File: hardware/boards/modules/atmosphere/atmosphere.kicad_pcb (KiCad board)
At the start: 2 copper layers, 95 x 75 mm, 18 parts, among them U7 ATtiny1614, U8 buffer

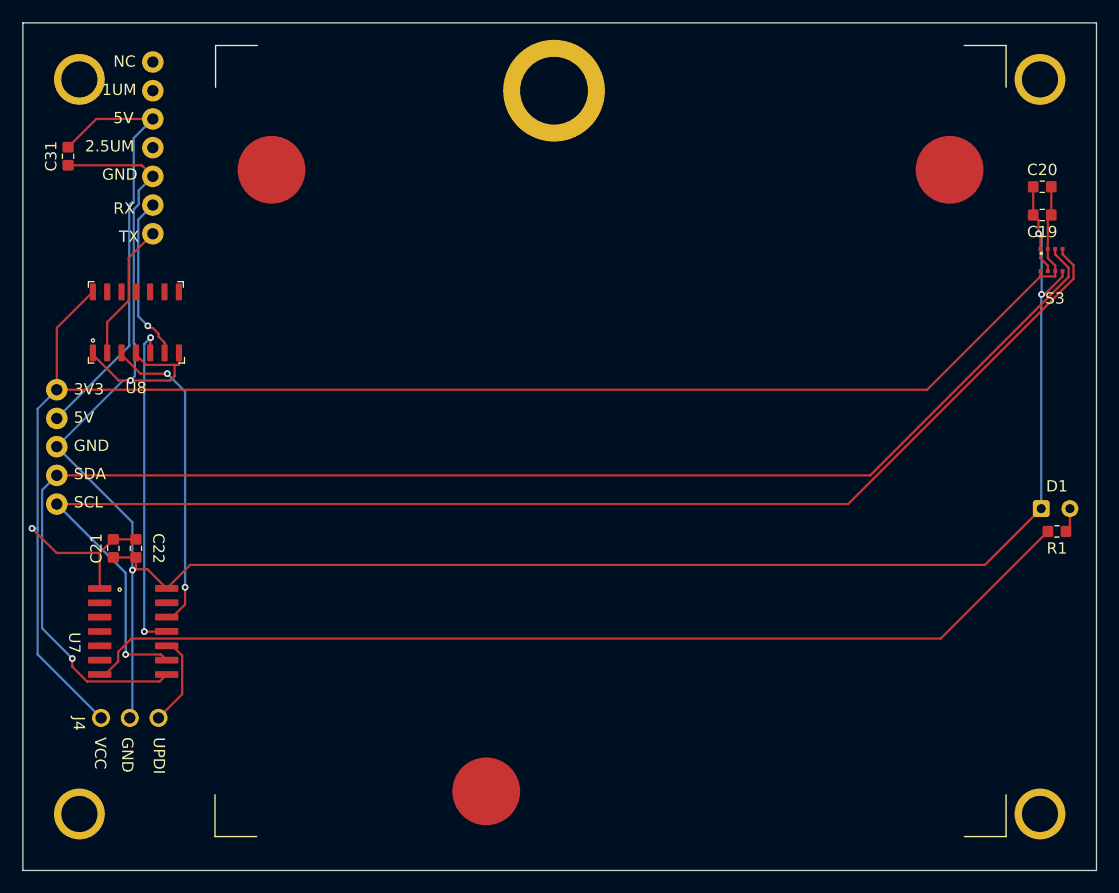
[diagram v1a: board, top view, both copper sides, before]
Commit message: updated sensor module schematics
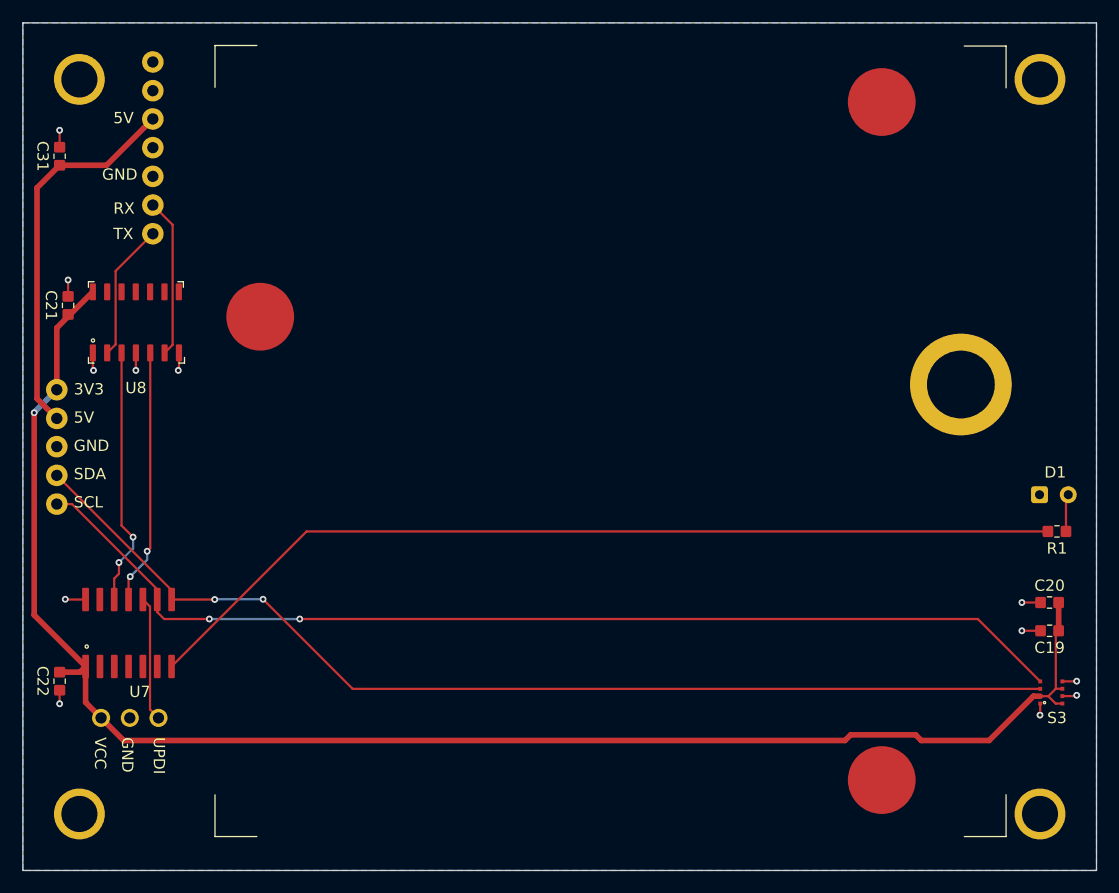
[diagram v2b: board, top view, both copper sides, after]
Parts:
- moved S3 38.3 mm to (203.0, 125.2), turned to 90 degrees
- moved C19 36.8 mm to (202.8, 119.8)
- moved C20 36.8 mm to (202.8, 117.3)
- moved C21 21.9 mm to (116.0, 91.0), turned to -90 degrees
- moved C22 13.6 mm to (115.2, 124.2)
- moved U7 7.93 mm to (122.3, 125.7), turned to 0 degrees
- moved D1 1.24 mm to (203.3, 110.8)
- moved C31 0.75 mm to (115.2, 77.8), turned to -90 degrees
- turned REF** to -90 degrees
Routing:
- net GND: track 200.1 -> 17.6 mm, vias 4 -> 12
- net SDA: track 127.5 -> 95.3 mm, vias 1 -> 2
- net SCL: track 120.9 -> 94.7 mm, vias 1 -> 2
- net 3V3: track 157.6 -> 142.7 mm
- net STATUS_LED: track 89.6 -> 82.5 mm
- net AT_CLIM_TX: track 29.6 -> 22.6 mm
- net AT_CLIM_RX: track 28.1 -> 22.9 mm
- net 5V: track 38.7 -> 33.9 mm
- net UPDI: track 8.11 -> 11.0 mm
- net Net-(D1-A): track 2.16 -> 3.33 mm
- net PM_RX: track 14.7 -> 14.1 mm, vias 1 -> 0
- added copper zone on B.Cu, net GND
